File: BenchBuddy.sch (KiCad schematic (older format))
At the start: 0 parts

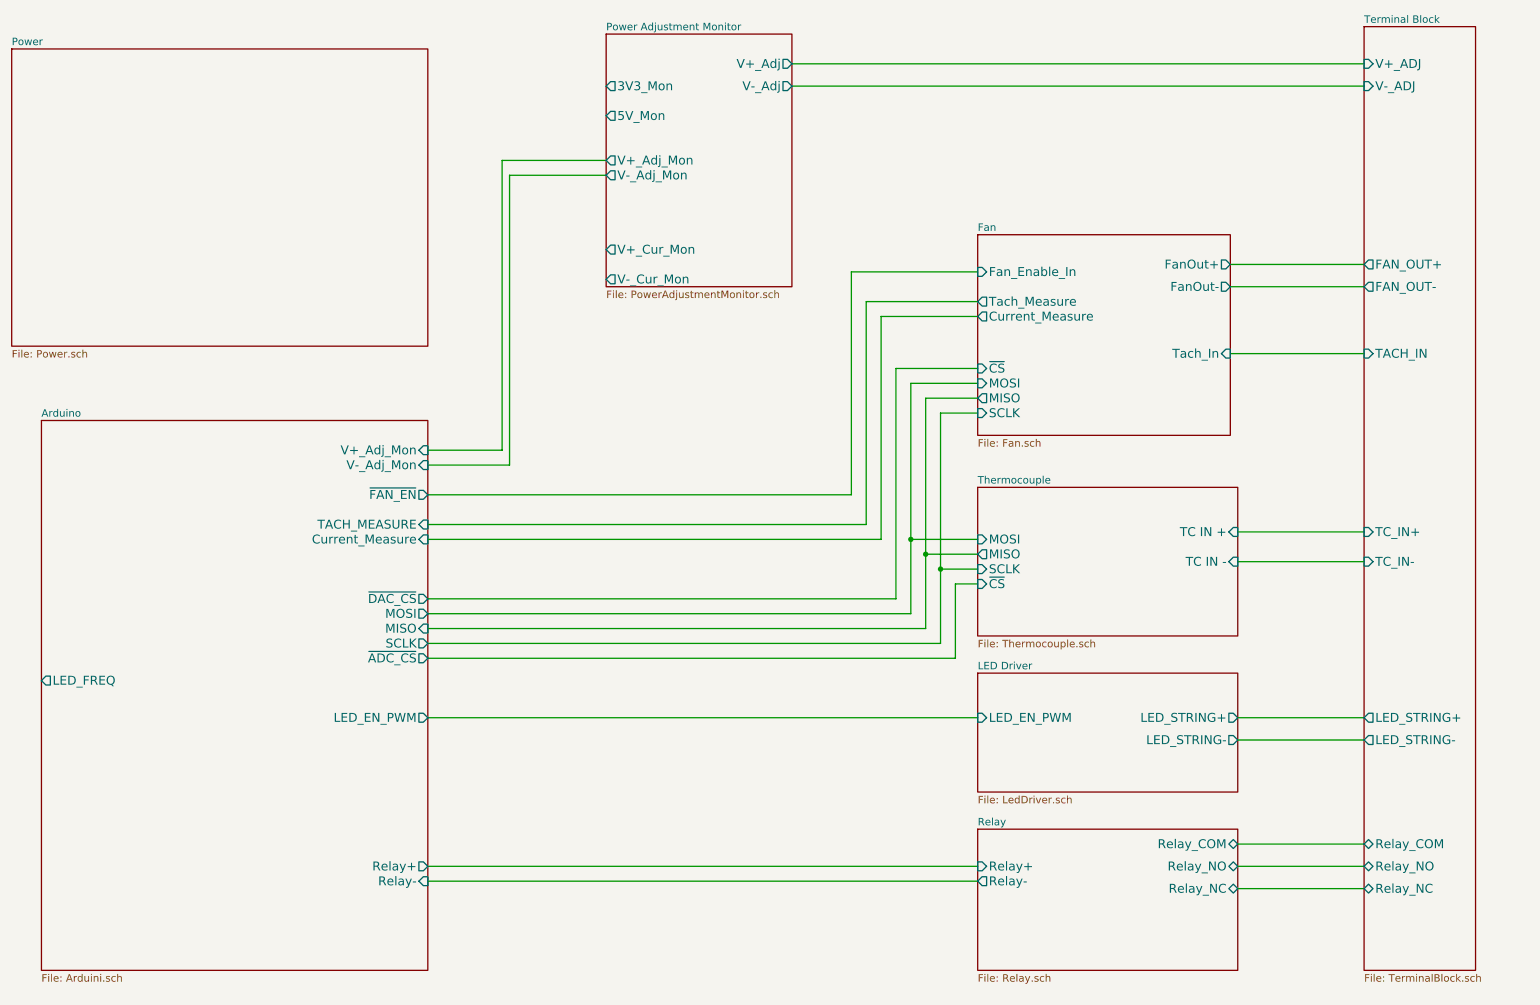
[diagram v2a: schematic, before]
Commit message: Fan/Current Module Refactor
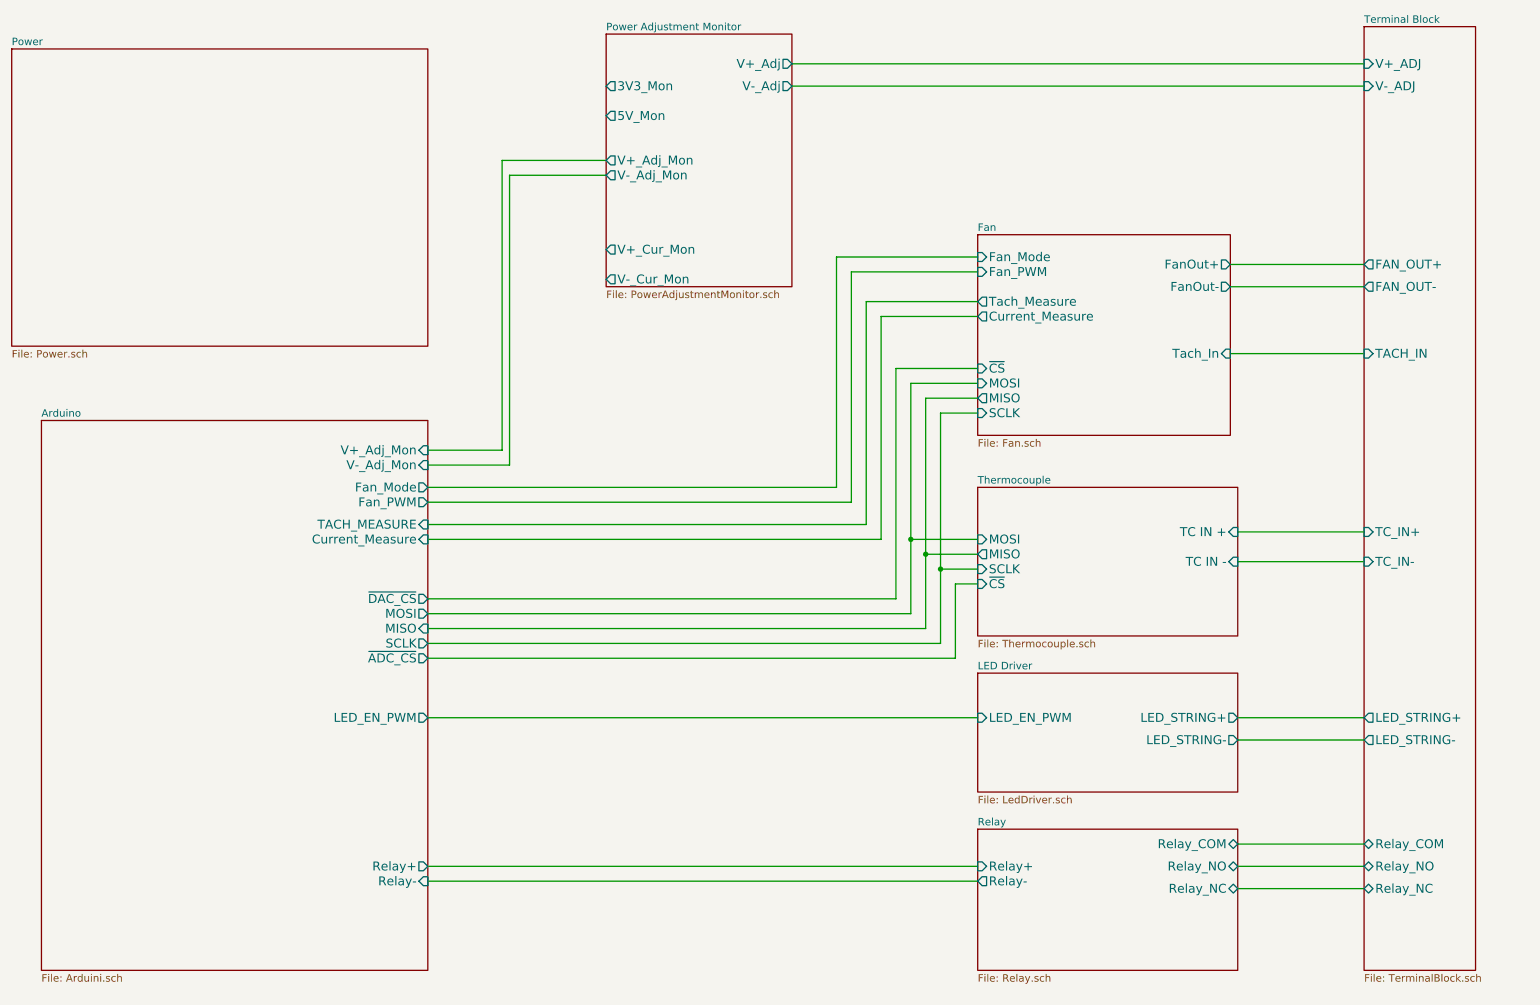
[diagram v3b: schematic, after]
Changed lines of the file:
@@
 Sheet 1 9
 Title ""
-Date "22 oct 2013"
+Date "23 oct 2013"
 Rev ""
 Comp ""
@@
 F8 "Tach_In" I R 9350 2850 60
 F9 "Tach_Measure" O L 7650 2500 60
-F10 "Fan_Enable_In" I L 7650 2300 60
-F11 "FanOut-" O R 9350 2400 60
+F10 "FanOut-" O R 9350 2400 60
+F11 "Fan_PWM" I L 7650 2300 60
+F12 "Fan_Mode" I L 7650 2200 60
 $EndSheet
 $Sheet
@@
 F5 "MISO" I R 3950 4700 60
 F6 "SCLK" O R 3950 4800 60
-F7 "LED_FREQ" O L 1350 5050 60
-F8 "TACH_MEASURE" I R 3950 4000 60
-F9 "~FAN_EN" O R 3950 3800 60
-F10 "Current_Measure" I R 3950 4100 60
-F11 "LED_EN_PWM" O R 3950 5300 60
-F12 "V+_Adj_Mon" I R 3950 3500 60
-F13 "V-_Adj_Mon" I R 3950 3600 60
-F14 "~DAC_CS" O R 3950 4500 60
-F15 "~ADC_CS" O R 3950 4900 60
+F7 "TACH_MEASURE" I R 3950 4000 60
+F8 "Current_Measure" I R 3950 4100 60
+F9 "LED_EN_PWM" O R 3950 5300 60
+F10 "V+_Adj_Mon" I R 3950 3500 60
+F11 "V-_Adj_Mon" I R 3950 3600 60
+F12 "~DAC_CS" O R 3950 4500 60
+F13 "~ADC_CS" O R 3950 4900 60
+F14 "Fan_Mode" O R 3950 3750 60
+F15 "Fan_PWM" O R 3950 3850 60
 $EndSheet
 Wire Wire Line
@@
 	7650 2300 6800 2300
 Wire Wire Line
-	6800 2300 6800 3800
-Wire Wire Line
-	6800 3800 3950 3800
+	6800 2300 6800 3850
 $Sheet
 S 10250 650  750  6350
@@
 Wire Wire Line
 	9400 4050 10250 4050
+Wire Wire Line
+	6800 3850 3950 3850
+Wire Wire Line
+	3950 3750 6700 3750
+Wire Wire Line
+	6700 3750 6700 2200
+Wire Wire Line
+	6700 2200 7650 2200
 $EndSCHEMATC
